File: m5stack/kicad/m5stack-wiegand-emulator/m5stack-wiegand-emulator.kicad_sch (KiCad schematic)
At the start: 4 parts, among them J1 2x15 socket header, J2 2x15 pin header, J3 1x5 female

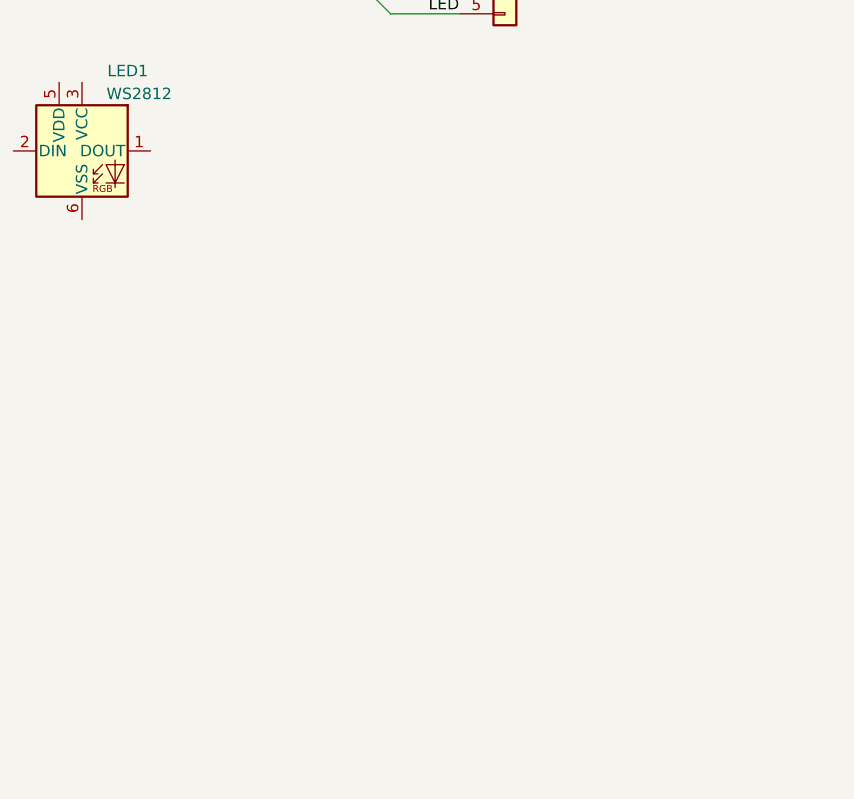
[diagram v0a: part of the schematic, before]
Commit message: M5: RP2040-Tiny symbol
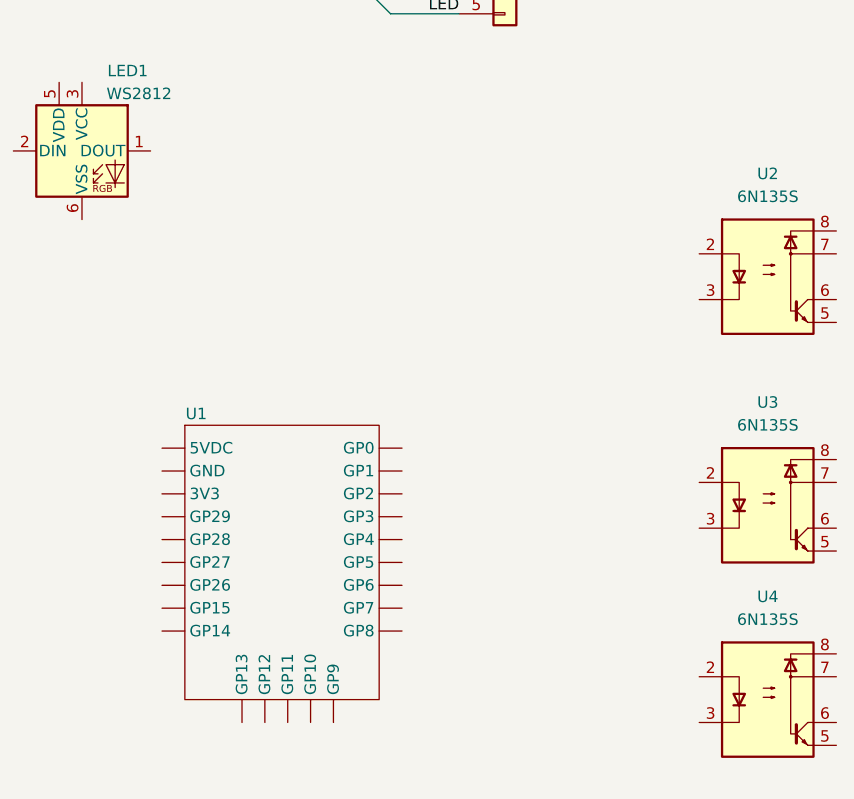
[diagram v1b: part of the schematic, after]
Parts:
- added U1: WaveShare RP2040-Tiny, symbol uhppoted:WaveShare_RP2040-Tiny
- added U2, U3, U4: 6N135S, Package_DIP:SMDIP-8_W9.53mm, symbol Isolator:6N135S
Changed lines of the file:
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@@
+    )
+  )
+  (symbol (lib_id "Isolator:6N135S") (at 181.61 114.3 0) (unit 1)
+    (in_bom yes) (on_board yes) (dnp no) (fields_autoplaced)
+    (property "Reference" "U4" (at 181.61 102.87 0)
+      (effects (font (size 1.27 1.27)))
+    )
+    (property "Value" "6N135S" (at 181.61 105.41 0)
+      (effects (font (size 1.27 1.27)))
+    )
+    (property "Footprint" "Package_DIP:SMDIP-8_W9.53mm" (at 176.53 121.92 0)
+      (effects (font (size 1.27 1.27) italic) (justify left) hide)
+    )
+    (property "Datasheet" "https://optoelectronics.liteon.com/upload/download/DS70-2008-0032/6N135-L%206N136-L%20series.pdf" (at 181.61 114.3 0)
+      (effects (font (size 1.27 1.27)) (justify left) hide)
+    )
+    (pin "4")
+    (pin "1")
+    (pin "2")
+    (pin "7")
+    (pin "8")
+    (pin "5")
+    (pin "3")
+    (pin "6")
+    (instances
+      (project "m5stack-wiegand-emulator"
+        (path "/591217c3-ab1f-4851-a185-c0f7ee9f3d97"
+          (reference "U4") (unit 1)
+        )
+      )
     )
   )
@@
     )
   )
+  (symbol (lib_id "uhppoted:WaveShare_RP2040-Tiny") (at 128.27 96.52 0) (unit 1)
+    (in_bom yes) (on_board yes) (dnp no)
+    (property "Reference" "U1" (at 118.11 82.55 0)
+      (effects (font (size 1.27 1.27)))
+    )
+    (property "Value" "WaveShare RP2040-Tiny" (at 127.635 81.28 0)
+      (effects (font (size 1.27 1.27)) hide)
+    )
+    (property "Footprint" "" (at 116.84 85.09 0)
+      (effects (font (size 1.27 1.27)) hide)
+    )
+    (property "Datasheet" "https://www.waveshare.com/wiki/RP2040-Tiny" (at 130.81 129.54 0)
+      (effects (font (size 1.27 1.27)) hide)
+    )
+    (pin "")
+    (pin "")
+    (pin "")
+    (pin "")
+    (pin "")
+    (pin "")
+    (pin "")
+    (pin "")
+    (pin "")
+    (pin "")
+    (pin "")
+    (pin "")
+    (pin "")
+    (pin "")
+    (pin "")
+    (pin "")
+    (pin "")
+    (pin "")
+    (pin "")
+    (pin "")
+    (pin "")
+    (pin "")
+    (pin "")
+    (instances
+      (project "m5stack-wiegand-emulator"
+        (path "/591217c3-ab1f-4851-a185-c0f7ee9f3d97"
+          (reference "U1") (unit 1)
+        )
+      )
+    )
+  )
   (symbol (lib_id "Connector_Generic:Conn_02x15_Odd_Even") (at 48.26 104.14 0) (unit 1)
     (in_bom yes) (on_board yes) (dnp no)
@@
         )
       )
+    )
+  )
+  (symbol (lib_id "Isolator:6N135S") (at 181.61 67.31 0) (unit 1)
+    (in_bom yes) (on_board yes) (dnp no) (fields_autoplaced)
+    (property "Reference" "U2" (at 181.61 55.88 0)
+      (effects (font (size 1.27 1.27)))
+    )
+    (property "Value" "6N135S" (at 181.61 58.42 0)
+      (effects (font (size 1.27 1.27)))
+    )
+    (property "Footprint" "Package_DIP:SMDIP-8_W9.53mm" (at 176.53 74.93 0)
+      (effects (font (size 1.27 1.27) italic) (justify left) hide)
+    )
+    (property "Datasheet" "https://optoelectronics.liteon.com/upload/download/DS70-2008-0032/6N135-L%206N136-L%20series.pdf" (at 181.61 67.31 0)
+      (effects (font (size 1.27 1.27)) (justify left) hide)
+    )
+    (pin "4")
+    (pin "2")
+    (pin "3")
+    (pin "6")
+    (pin "5")
+    (pin "8")
+    (pin "7")
+    (pin "1")
+    (instances
+      (project "m5stack-wiegand-emulator"
+        (path "/591217c3-ab1f-4851-a185-c0f7ee9f3d97"
+          (reference "U2") (unit 1)
+        )
+      )
+    )
+  )
+  (symbol (lib_id "Isolator:6N135S") (at 181.61 92.71 0) (unit 1)
+    (in_bom yes) (on_board yes) (dnp no) (fields_autoplaced)
+    (property "Reference" "U3" (at 181.61 81.28 0)
+      (effects (font (size 1.27 1.27)))
+    )
+    (property "Value" "6N135S" (at 181.61 83.82 0)
+      (effects (font (size 1.27 1.27)))
+    )
+    (property "Footprint" "Package_DIP:SMDIP-8_W9.53mm" (at 176.53 100.33 0)
+      (effects (font (size 1.27 1.27) italic) (justify left) hide)
+    )
+    (property "Datasheet" "https://optoelectronics.liteon.com/upload/download/DS70-2008-0032/6N135-L%206N136-L%20series.pdf" (at 181.61 92.71 0)
+      (effects (font (size 1.27 1.27)) (justify left) hide)
+    )
+    (pin "3")
+    (pin "8")
+    (pin "4")
+    (pin "7")
+    (pin "5")
+    (pin "6")
+    (pin "1")
+    (pin "2")
+    (instances
+      (project "m5stack-wiegand-emulator"
+        (path "/591217c3-ab1f-4851-a185-c0f7ee9f3d97"
+          (reference "U3") (unit 1)
+        )
+      )

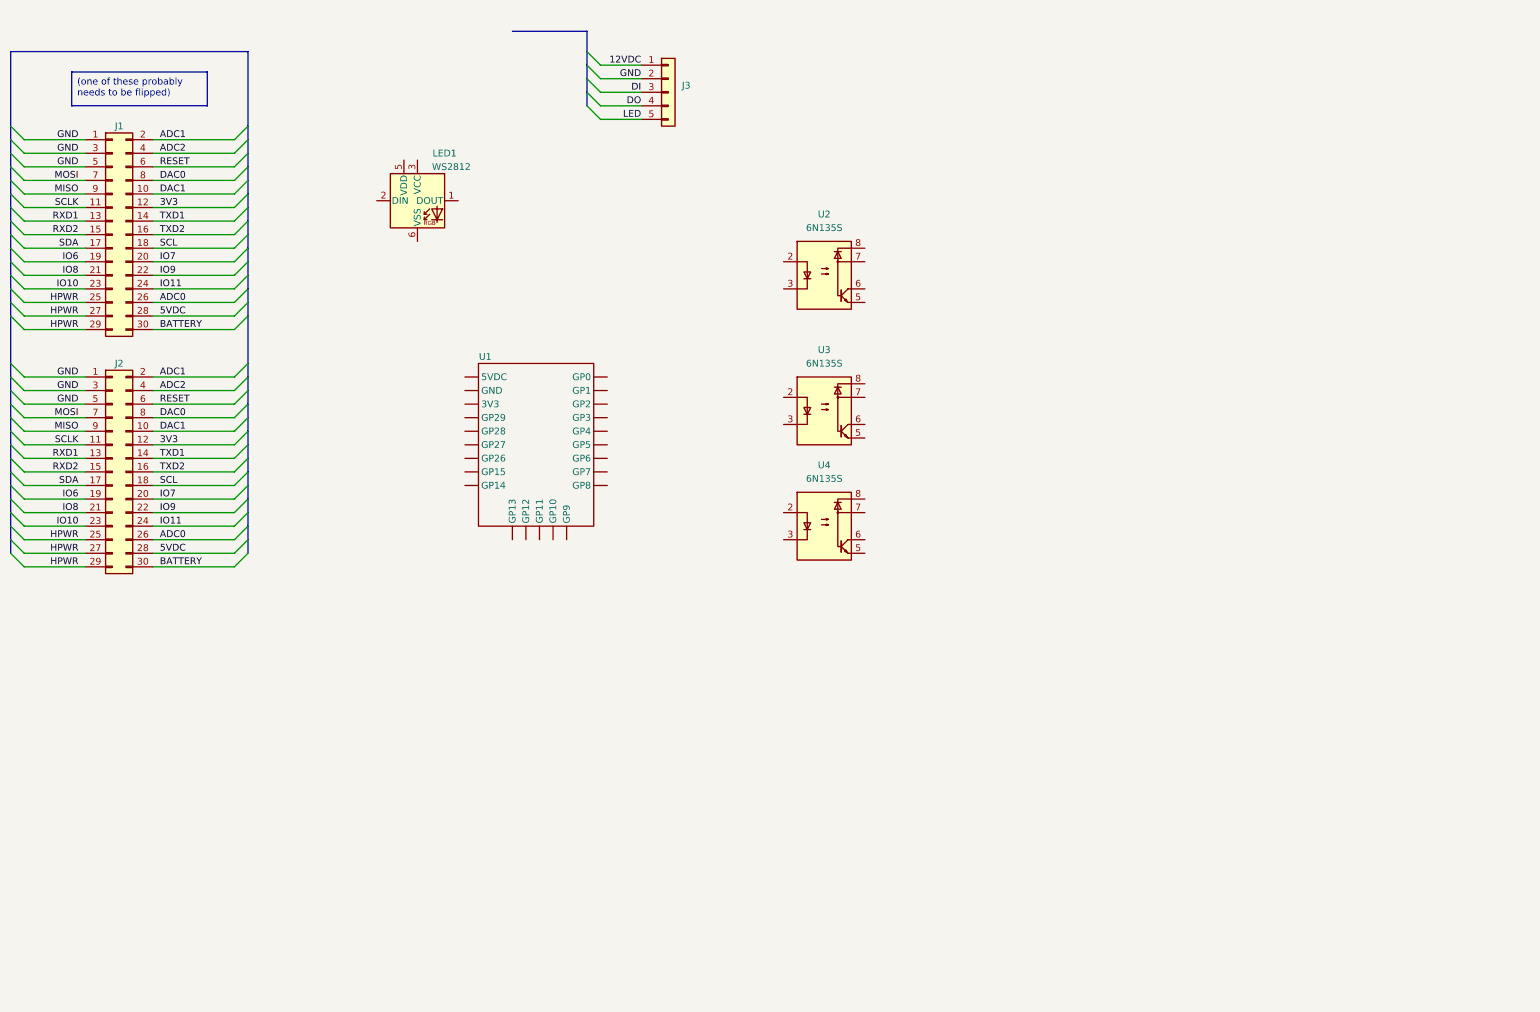
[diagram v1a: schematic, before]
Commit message: M5: added opto-isolators
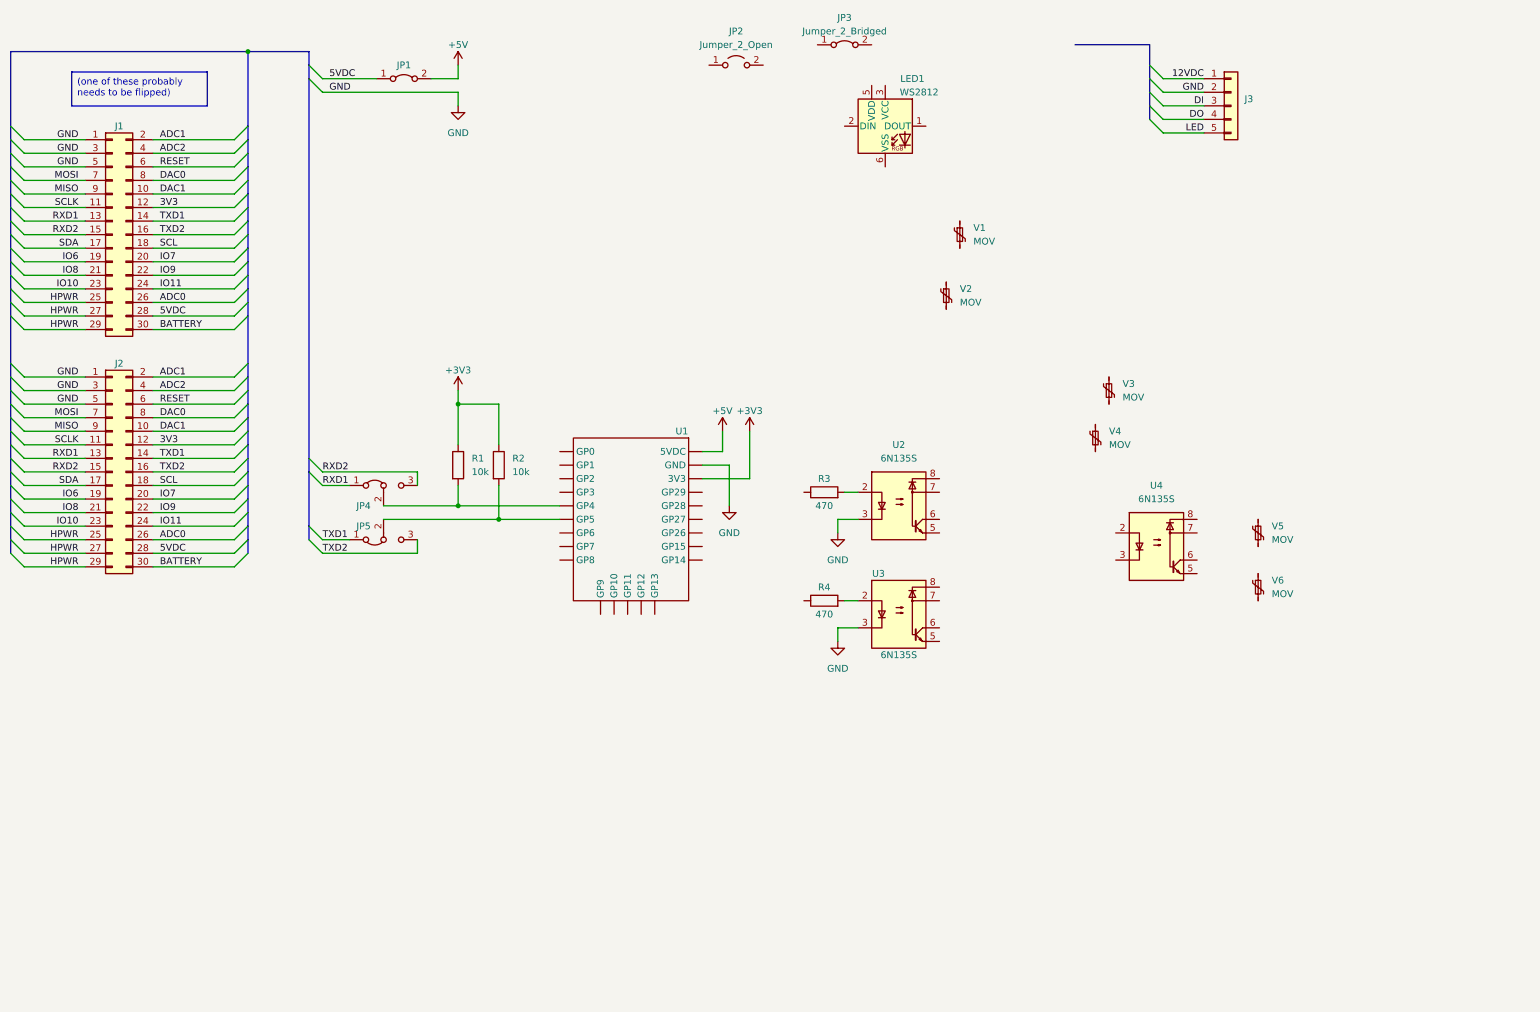
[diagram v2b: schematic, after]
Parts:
- added JP1, JP3: Jumper_2_Bridged, symbol Jumper:Jumper_2_Bridged
- added JP2: Jumper_2_Open, symbol Jumper:Jumper_2_Open
- added JP4, JP5: Jumper_3_Bridged12, symbol Jumper:Jumper_3_Bridged12
- added R1, R2: 10k, symbol Device:R
- added R3, R4: 470, symbol Device:R
- added V1, V2, V3, V4, V5, V6: MOV, symbol uhppoted:MOV
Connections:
- net 5VDC: now also JP1.1 (A)
- net GND: now also U1. (GP9), U2.3, U3.3
- net RXD1: now also JP4.1 (A)
- net RXD2: now also JP4.3 (B)
- net TXD1: now also JP5.1 (A)
- net TXD2: now also JP5.3 (B)
- net at U2.2: now also R3.2
- net at U3.2: now also R4.2
- new net: JP5.2 (C), R2.2, U1. (GP9)
- new net: JP4.2 (C), R1.2, U1. (GP9)
- new net +3V3: R1.1, R2.1, U1. (GP9)
- new net +5V: JP1.2 (B), U1. (GP9)
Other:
- moved on the sheet: J3, LED1, U1, U2, U3, U4

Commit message: m5stack: yet more application notes
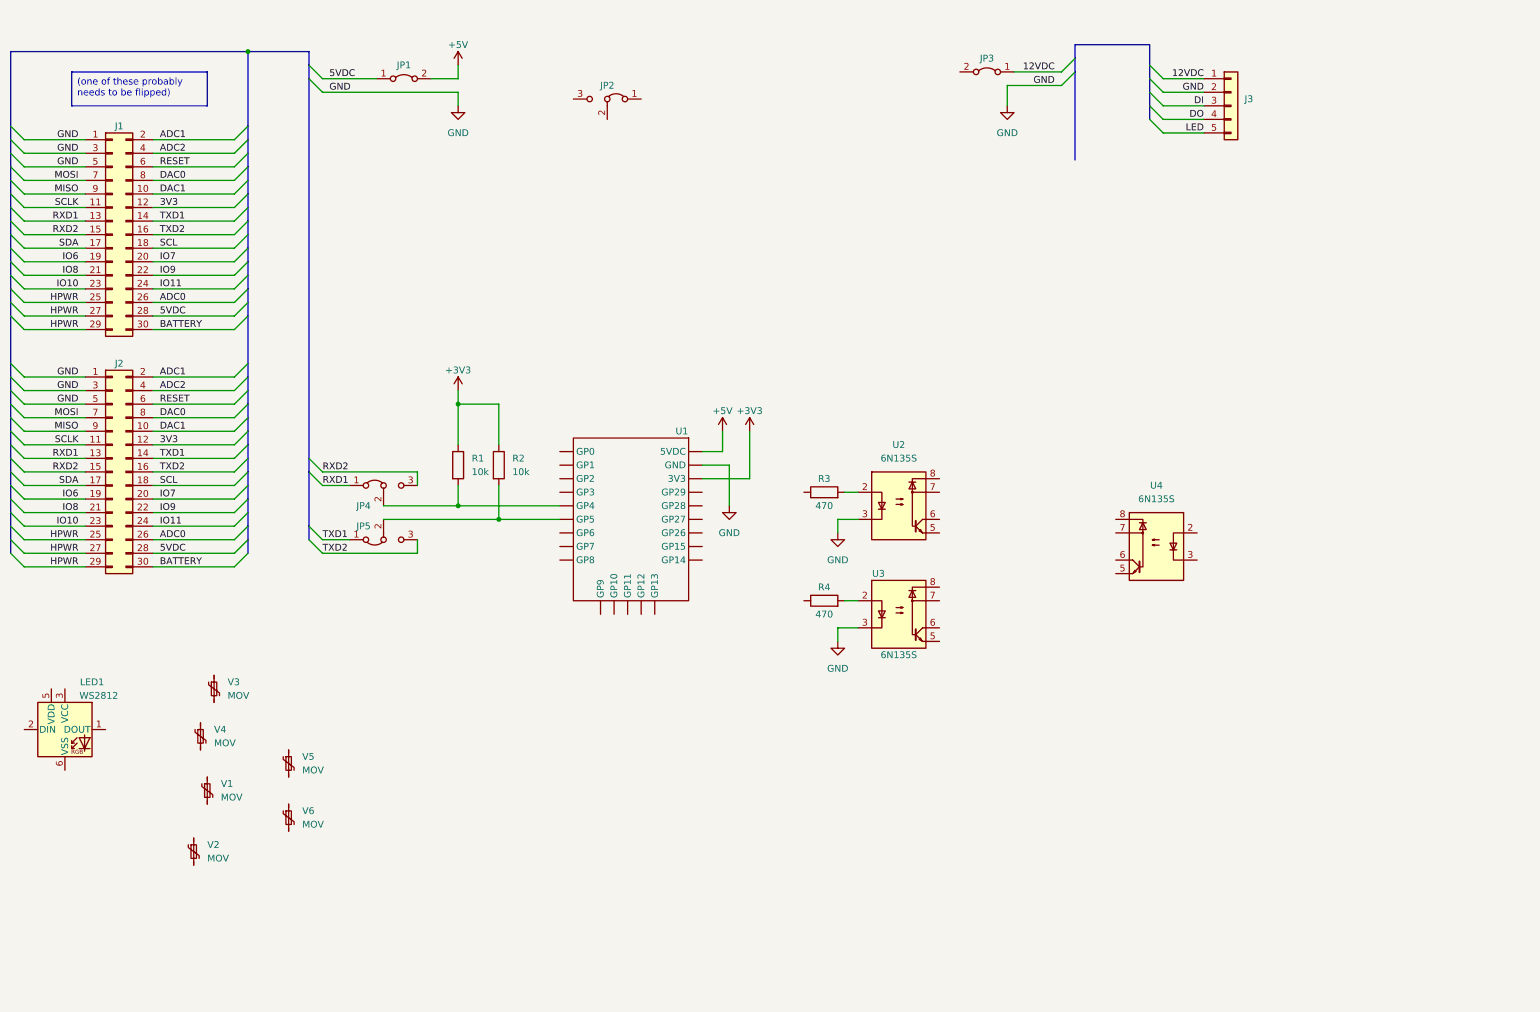
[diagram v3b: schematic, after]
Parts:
- JP2: value Jumper_2_Open -> Jumper_3_Bridged12; symbol Jumper:Jumper_2_Open -> Jumper:Jumper_3_Bridged12
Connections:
- net 12VDC: now also JP3.1 (A)
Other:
- moved on the sheet: JP3, LED1, V1, V2, V3, V4, V5, V6

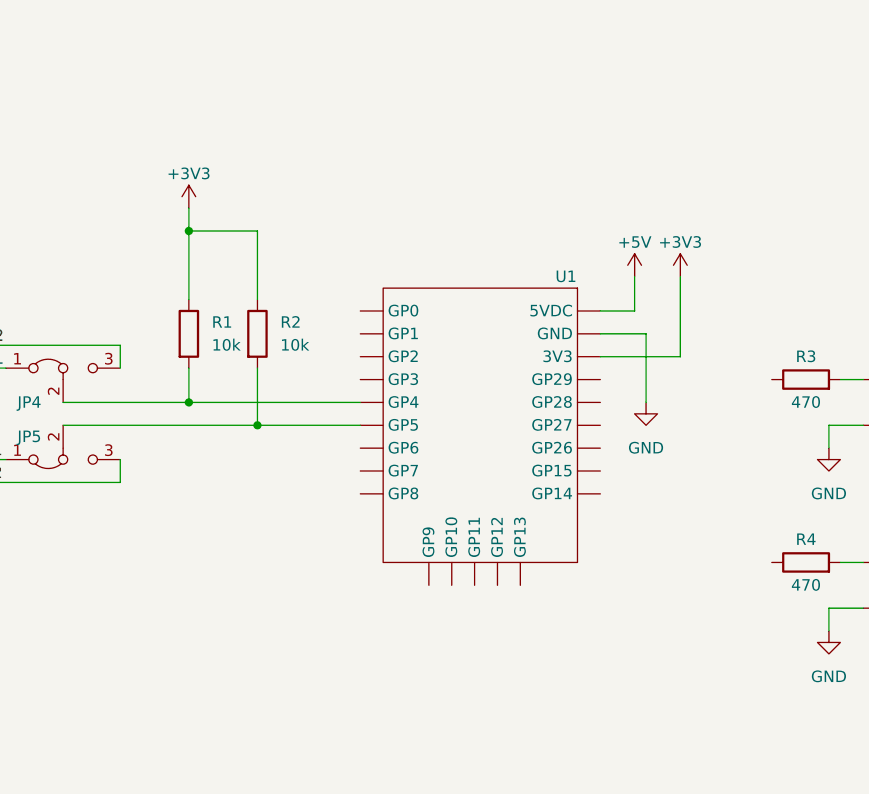
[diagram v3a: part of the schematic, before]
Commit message: M5: reworked RP2040-Tiny symbol
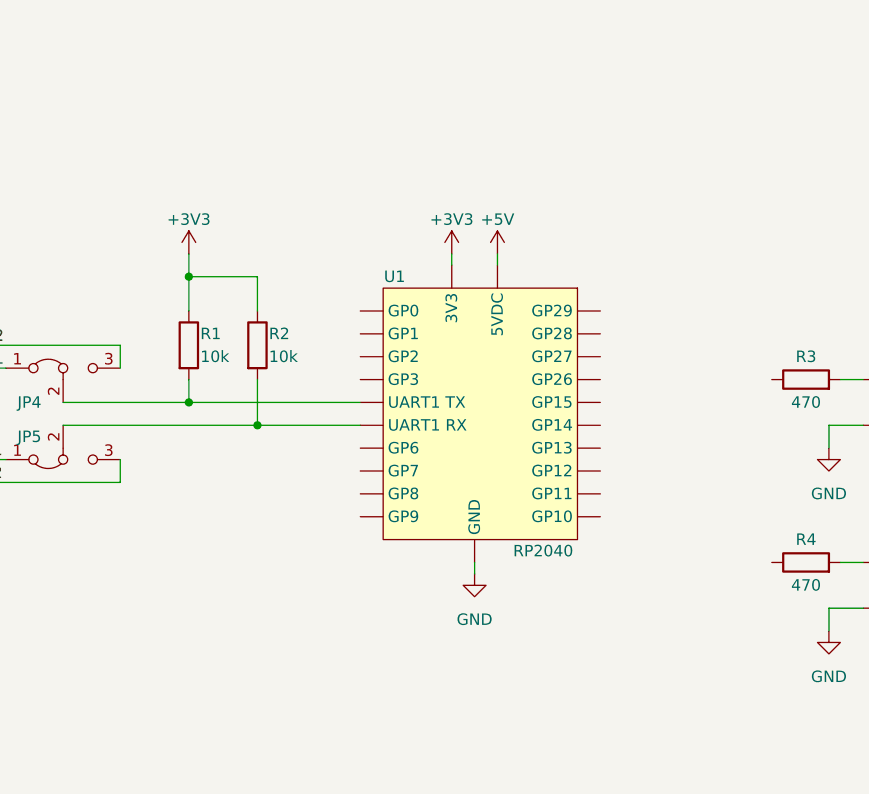
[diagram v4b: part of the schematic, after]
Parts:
- U1: value WaveShare RP2040-Tiny -> RP2040
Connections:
- net +3V3: now also U1.3 (3V3); no longer U1. (GP9)
- net +5V: now also U1.1 (5VDC); no longer U1. (GP9)
- net GND: now also U1.2 (GND); no longer U1. (GP9)
- net at JP5.2 (C), R2.2: now also U1.18 (GP5); no longer U1. (GP9)
- net at JP4.2 (C), R1.2: now also U1.19 (GP4); no longer U1. (GP9)
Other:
- moved on the sheet: R1, R2
